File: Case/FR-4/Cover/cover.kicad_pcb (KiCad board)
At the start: 2 copper layers, 19.1 x 56.7 mm, 0 parts

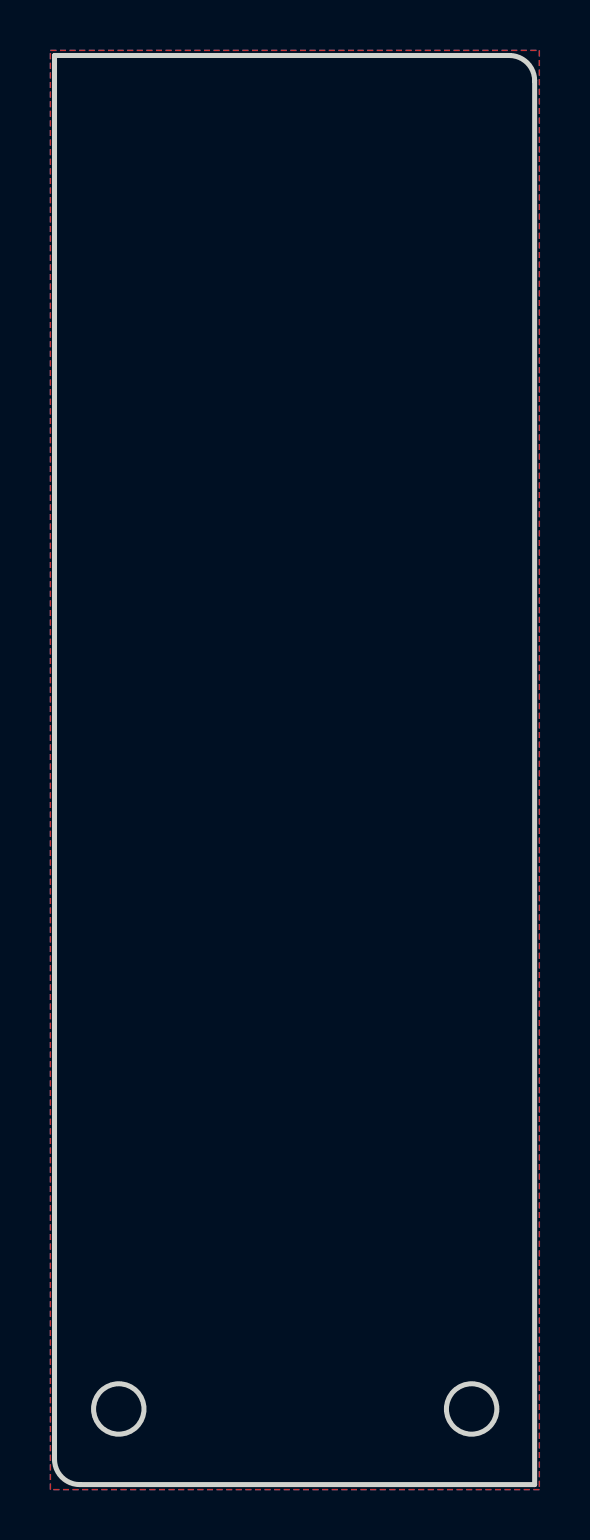
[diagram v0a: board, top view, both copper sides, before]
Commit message: Create files for FR-4 cover
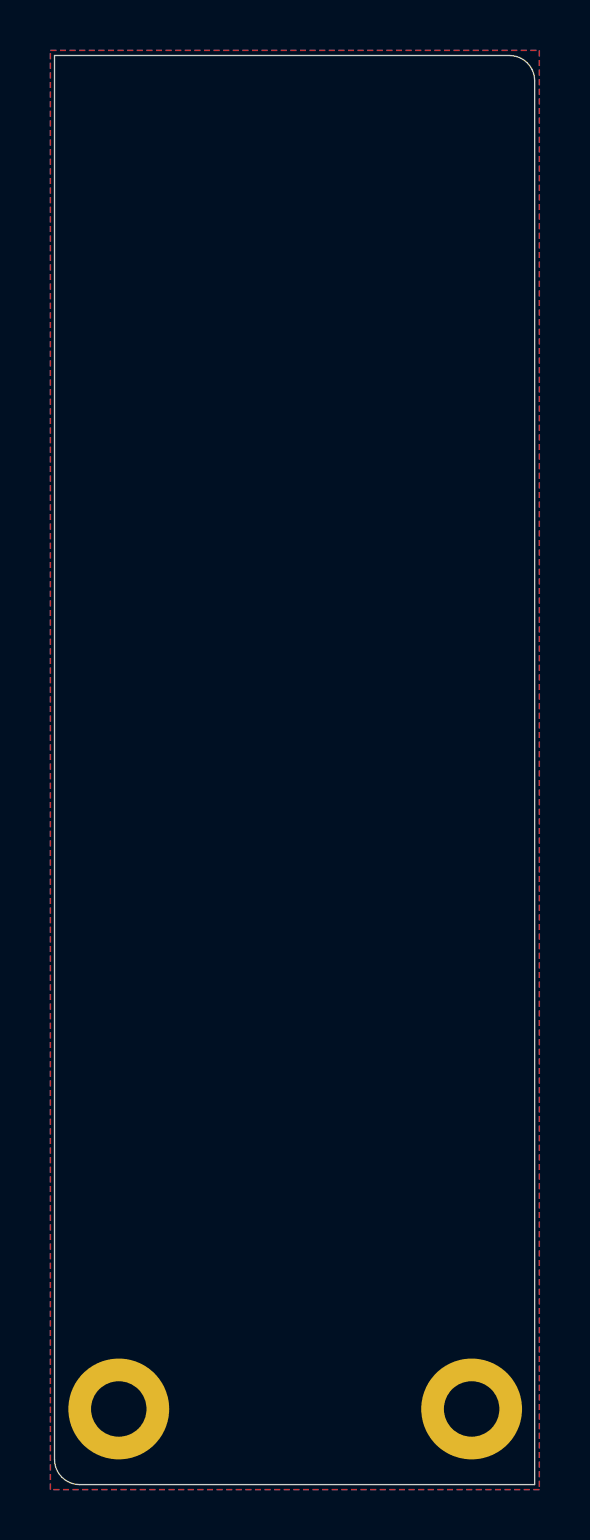
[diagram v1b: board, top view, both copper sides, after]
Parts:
- added REF**: Hole_Cover_M2, Used_Footprints:Hole_Cover_M2, F.Cu at (169.9, 134.7)
- added REF**: Hole_Cover_M2, Used_Footprints:Hole_Cover_M2, F.Cu at (155.9, 134.7)
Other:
- outline, holes or cut-outs redrawn
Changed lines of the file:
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@@
   (general
     (thickness 1.6)
-    (drawings 8)
+    (drawings 6)
     (tracks 0)
     (zones 0)
-    (modules 0)
+    (modules 2)
     (nets 1)
   )
@@
     (solder_mask_min_width 0.25)
     (aux_axis_origin 0 0)
-    (visible_elements FFFFFF7F)
+    (visible_elements 7FFFFFFF)
     (pcbplotparams
       (layerselection 0x010f0_ffffffff)
@@
       (drillshape 0)
       (scaleselection 1)
-      (outputdirectory ""))
+      (outputdirectory "Gerbers/"))
   )
   (net 0 "")
@@
     (uvia_drill 0.1)
   )
-  (gr_arc (start 171.41242 82.001478) (end 172.41242 82.001478) (angle -90) (layer Edge.Cuts) (width 0.2))
-  (gr_line (start 171.41242 81.001478) (end 153.36242 81.001478) (layer Edge.Cuts) (width 0.2))
-  (gr_circle (center 169.91242 134.701478) (end 168.91242 134.701478) (layer Edge.Cuts) (width 0.2))
-  (gr_line (start 153.36242 136.701478) (end 153.36242 81.001478) (layer Edge.Cuts) (width 0.2))
-  (gr_circle (center 155.91242 134.701478) (end 154.91242 134.701478) (layer Edge.Cuts) (width 0.2))
-  (gr_line (start 172.41242 137.701478) (end 172.41242 82.001478) (layer Edge.Cuts) (width 0.2))
-  (gr_line (start 154.36242 137.701478) (end 172.41242 137.701478) (layer Edge.Cuts) (width 0.2))
-  (gr_arc (start 154.36242 136.701478) (end 153.36242 136.701478) (angle -90) (layer Edge.Cuts) (width 0.2))
+  (module Used_Footprints:Hole_Cover_M2 (layer F.Cu)
+    (at 169.91242 134.701478)
+    (fp_text reference REF** (at -0.26242 -3.571478) (layer F.SilkS) hide
+      (effects (font (size 1 1) (thickness 0.15)))
+    )
+    (fp_text value Hole_Cover_M2 (at -4.08242 -2.761478 90) (layer F.Fab) hide
+      (effects (font (size 1 1) (thickness 0.15)))
+    )
+    (pad 1 thru_hole circle (at 0 0) (size 4 4) (drill 2.2) (layers *.Cu *.Mask))
+  )
+  (module Used_Footprints:Hole_Cover_M2 (layer F.Cu)
+    (at 155.91242 134.701478)
+    (fp_text reference REF** (at 0.42758 -3.761478) (layer F.SilkS) hide
+      (effects (font (size 1 1) (thickness 0.15)))
+    )
+    (fp_text value Hole_Cover_M2 (at 3.72758 -2.581478 90) (layer F.Fab) hide
+      (effects (font (size 1 1) (thickness 0.15)))
+    )
+    (pad 1 thru_hole circle (at 0 0) (size 4 4) (drill 2.2) (layers *.Cu *.Mask))
+  )
+  (gr_arc (start 171.41242 82.001478) (end 172.41242 82.001478) (angle -90) (layer Edge.Cuts) (width 0.05))
+  (gr_arc (start 154.36242 136.701478) (end 153.36242 136.701478) (angle -90) (layer Edge.Cuts) (width 0.05))
+  (gr_line (start 171.41242 81.001478) (end 153.36242 81.001478) (layer Edge.Cuts) (width 0.05))
+  (gr_line (start 153.36242 136.701478) (end 153.36242 81.001478) (layer Edge.Cuts) (width 0.05))
+  (gr_line (start 172.41242 137.701478) (end 172.41242 82.001478) (layer Edge.Cuts) (width 0.05))
+  (gr_line (start 154.36242 137.701478) (end 172.41242 137.701478) (layer Edge.Cuts) (width 0.05))
   (zone (net 0) (net_name "") (layer F.Cu) (hatch edge 0.508)
     (connect_pads (clearance 0.508))

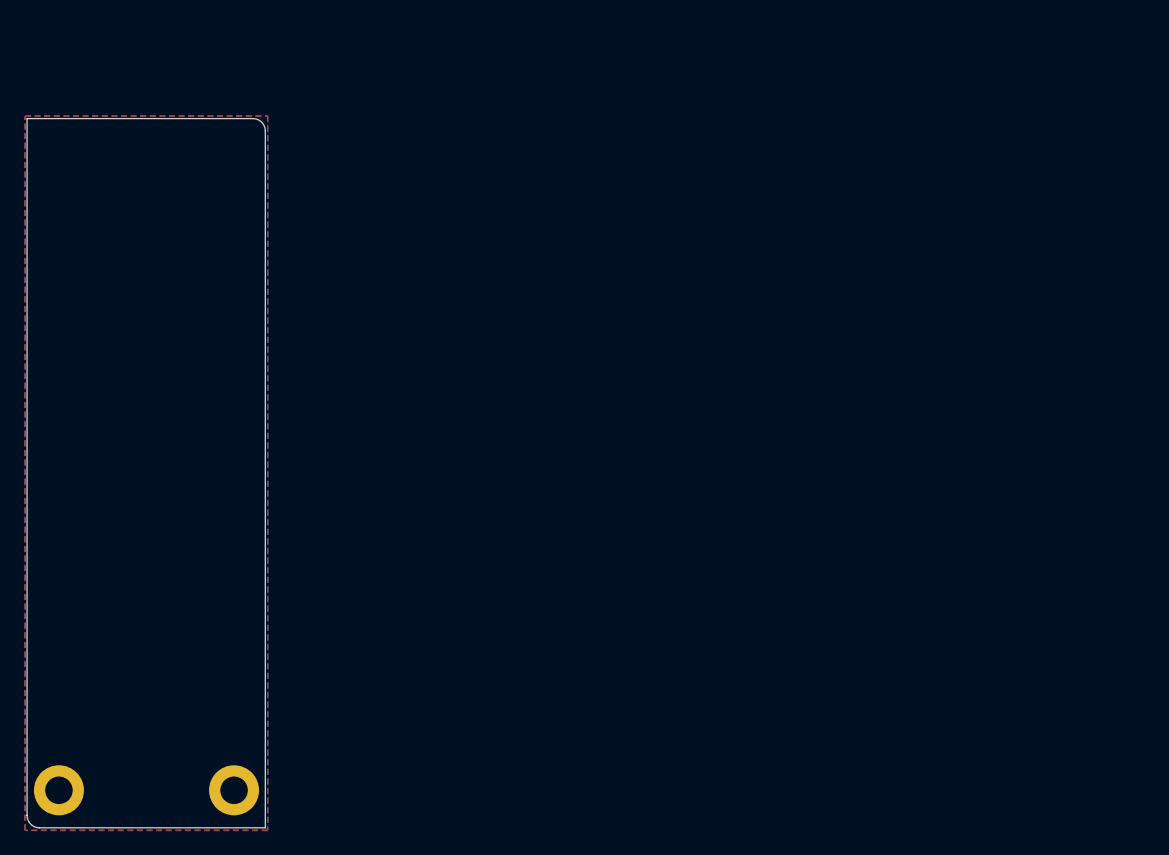
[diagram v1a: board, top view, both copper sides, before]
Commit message: Add silk at PCB
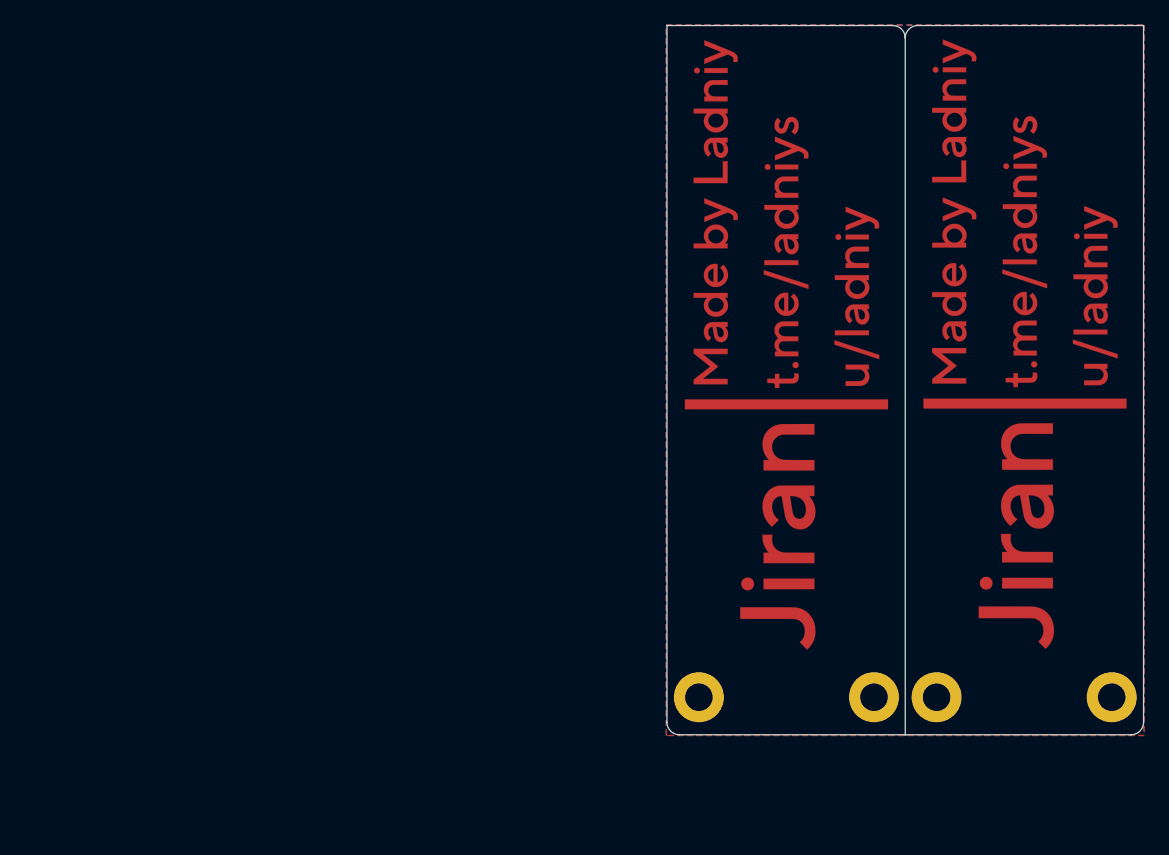
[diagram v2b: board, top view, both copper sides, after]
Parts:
- removed the REF** at (169.9, 134.7)
- removed the REF** at (155.9, 134.7)
- added G***: LOGO, Used_Footprints:Silk_Cover, F.Cu at (233.1, 101.6)
- added G***: LOGO, Used_Footprints:Silk_Cover, F.Cu at (214.1, 101.7)
- added REF**: Hole_Cover_M2, Used_Footprints:Hole_Cover_M2, B.Cu at (226.1, 127.3)
- added REF**: Hole_Cover_M2, Used_Footprints:Hole_Cover_M2, B.Cu at (240.1, 127.3)
- added REF**: Hole_Cover_M2, Used_Footprints:Hole_Cover_M2, F.Cu at (221.1, 127.3)
- added REF**: Hole_Cover_M2, Used_Footprints:Hole_Cover_M2, F.Cu at (207.1, 127.3)
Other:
- board size 19.1 x 56.7 mm -> 38.1 x 56.7 mm
